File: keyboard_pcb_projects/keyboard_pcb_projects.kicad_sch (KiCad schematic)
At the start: 21 parts, among them J1 AVR-ISP-6, SW1 SW_Push_Reset, U1 ATmega32U4-A, Y1 Crystal_GND24_Small

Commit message: More wiring progress
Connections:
- net +5V: now also C5.1, C6.1, C7.1, C8.1
- net at USB1.10 (CC2): now also R6.1; no longer R5.1
- net at USB1.4 (CC1): now also R5.1; no longer R6.1

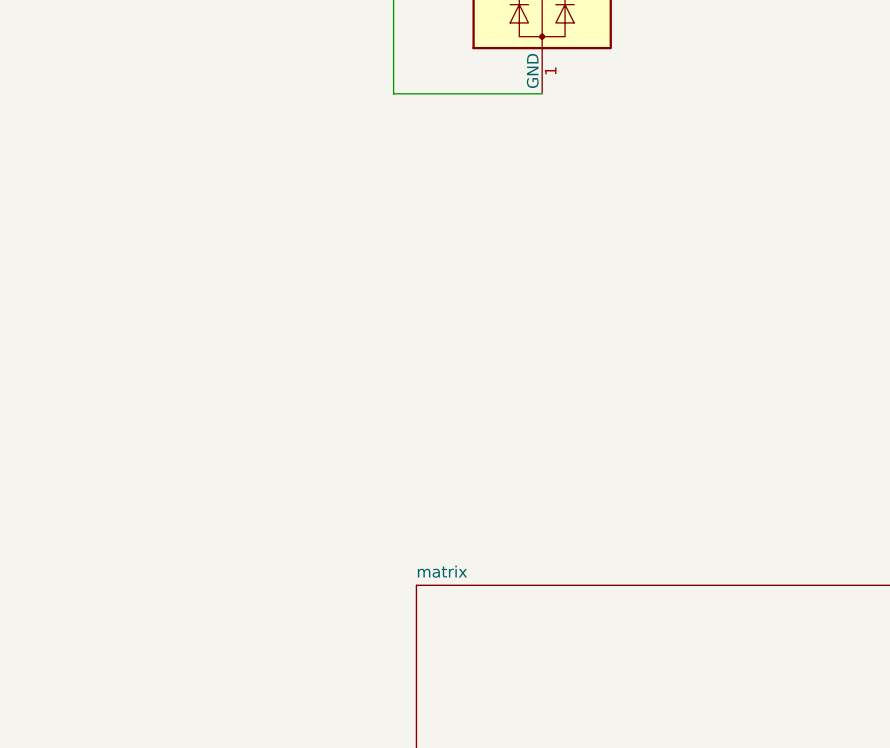
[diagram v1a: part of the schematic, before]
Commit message: Added copper padded mounting hole and exported STEP file for the board
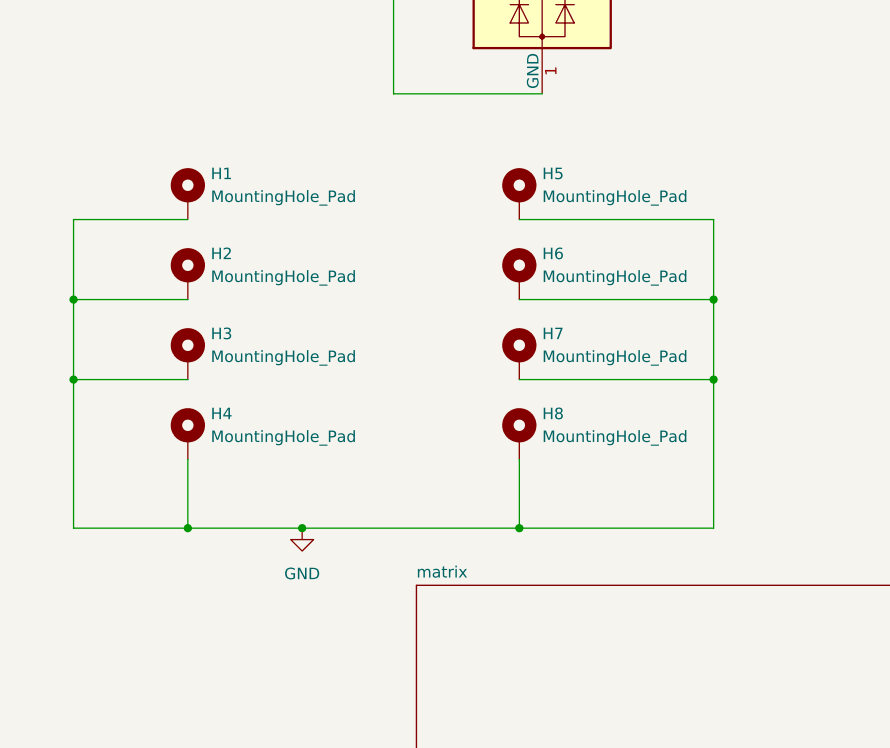
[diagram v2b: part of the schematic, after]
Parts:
- added H1, H2, H3, H4, H5, H6, H7, H8: MountingHole_Pad, MountingHole:MountingHole_2.2mm_M2_Pad, symbol Mechanical:MountingHole_Pad
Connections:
- net GND: now also H1.1, H2.1, H3.1, H4.1, H5.1, H6.1, H7.1, H8.1
